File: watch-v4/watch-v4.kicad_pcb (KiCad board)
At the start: 4 copper layers, 35 x 35 mm, 33 parts, among them J1 CONN_10, P1 array connection, Q1 MOSFET_P, SW1 SPST, SW2 SPST, SW3 SPST, U1 IC_MCP73831, U2 MAX1722, U3 DS3231, U4 LSM9DS0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

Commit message: schematic cleanup, board work
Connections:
- net Net-(D2-Pad2) renamed /STAT
- D1 pad 1: Net-(D1-Pad1) -> /EXTVCC
- D1 pad 2: Net-(D1-Pad2) -> /Regulator_In
- J1 pad 4: Net-(J1-Pad4) -> VCC
- L1 pad 1: Net-(D1-Pad2) -> /Regulator_In
- P1 pad 1: EXTVCC -> /EXTVCC
- Q1 pad 1: EXTVCC -> /EXTVCC
- Q1 pad 3: Net-(D1-Pad2) -> /Regulator_In
- R1 pad 2: EXTVCC -> /EXTVCC
- R3 pad 1: Net-(D1-Pad1) -> /EXTVCC
- U1 pad 4: EXTVCC -> /EXTVCC
- U2 pad 1: Net-(D1-Pad2) -> /Regulator_In
- U2 pad 3: Net-(U2-Pad3) -> /Regulator_In
- XL1 pad 1: EXTVCC -> /EXTVCC
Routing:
- net /EXTVCC: track 0.00 -> 50.4 mm, vias 0 -> 1
- net EXTVCC: track 47.2 -> 0.00 mm, vias 1 -> 0
- net /Regulator_In: track 0.00 -> 15.7 mm
- net Net-(D1-Pad2): track 11.6 -> 0.00 mm
- net Net-(D1-Pad1): track 3.24 -> 0.00 mm
- net VCC: track 113.7 -> 114.2 mm

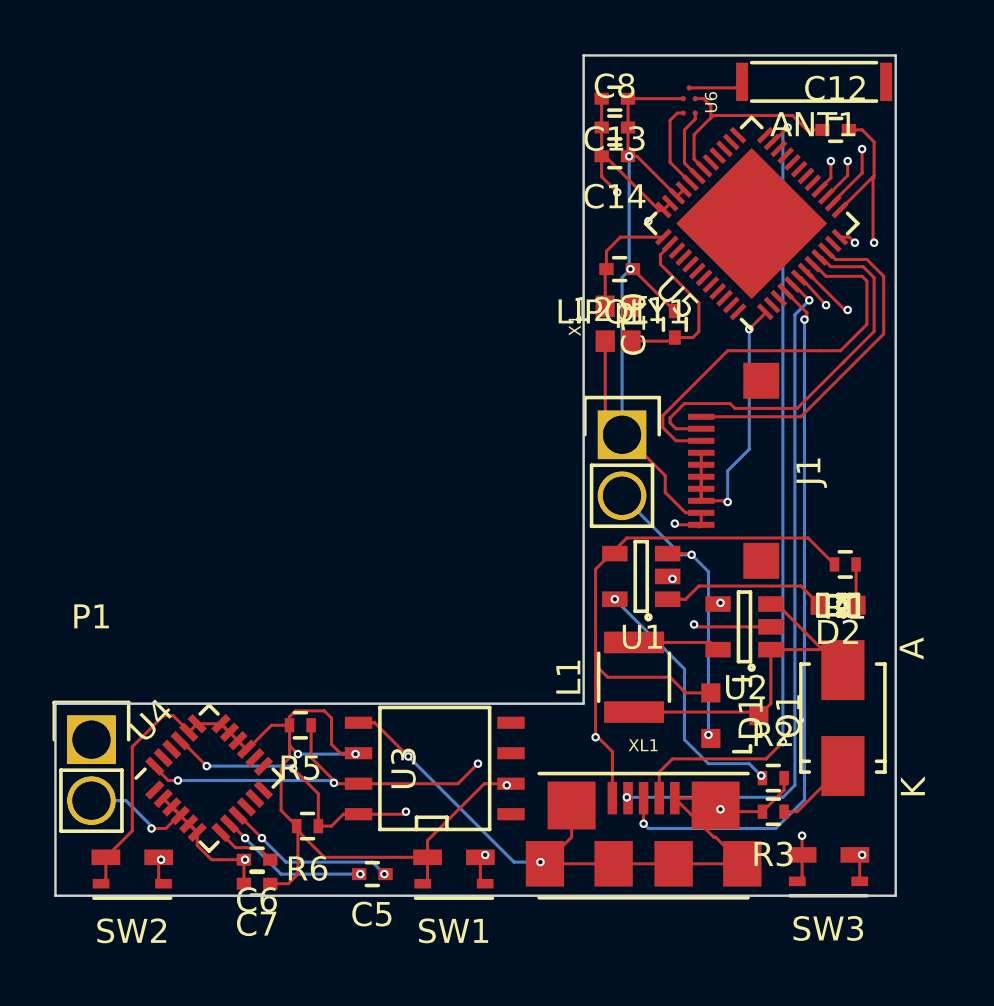
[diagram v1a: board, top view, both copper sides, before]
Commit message: re-route board, redraw power supply in schematic
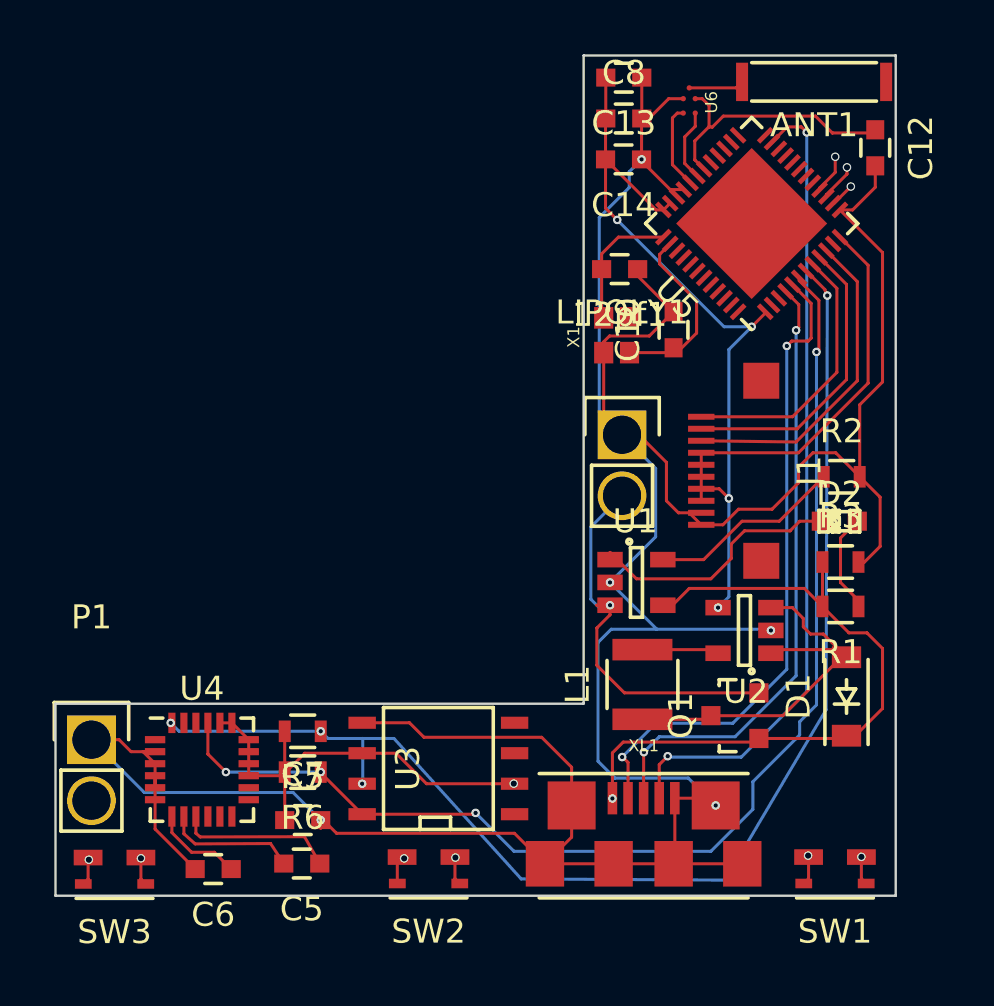
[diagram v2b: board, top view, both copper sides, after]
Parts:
- 12pf1, C10, C12, C13, C14, C5, C6, C7, C8: footprint Capacitors_SMD:C_0402 -> Capacitors_SMD:C_0603
- D1: footprint Diodes_SMD:Diode-SMA_Standard -> Diodes_SMD:SOD-123
- R1, R2, R3, R5, R6: footprint Resistors_SMD:R_0402 -> Resistors_SMD:R_0603
- moved SW3 29.7 mm to (152.7, 114.4)
- moved SW1 15.9 mm to (182.7, 114.4)
- moved R2 12.9 mm to (182.9, 98.2)
- moved SW2 12.3 mm to (165.7, 114.4)
- moved R3 10.8 mm to (182.9, 101.8), turned to 0 degrees
- moved D2 3.50 mm to (182.8, 100.1), turned to 0 degrees
- moved C7 3.26 mm to (160.5, 112.5), turned to 0 degrees
- moved C5 2.97 mm to (160.5, 114.4)
- moved R6 2.26 mm to (160.5, 110.5)
- moved C6 1.87 mm to (156.8, 114.6)
- moved C12 1.81 mm to (184.3, 84.5), turned to 270 degrees
- moved R1 1.76 mm to (182.9, 103.7)
- moved C13 0.95 mm to (173.9, 81.6)
- moved D1 0.91 mm to (183.2, 107.4)
- moved C8 0.53 mm to (173.9, 83.3)
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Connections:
- net Net-(LIPOLY1-Pad2) renamed /VBAT
- D2 pad 2: /STAT -> Net-(D2-Pad2)
- P1 pad 1: /EXTVCC -> GND
- P1 pad 2: GND -> /EXTVCC
- R1 pad 1: Net-(D2-Pad1) -> Net-(D2-Pad2)
- U1 pad 1: /STAT -> Net-(D2-Pad1)
- U5 pad 10: DISPLAY_SCK -> DISPLAY_SS
- U5 pad 8: DISPLAY_SS -> DISPLAY_SCK
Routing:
- net GND: track 128.8 -> 150.3 mm, vias 11 -> 5
- net Net-(SW3-Pad2): track 35.3 -> 52.4 mm
- net Net-(SW1-Pad2): track 44.5 -> 30.3 mm
- net Net-(SW2-Pad2): track 53.4 -> 39.3 mm
- net VCC: track 114.2 -> 127.8 mm, vias 10 -> 8
- net Net-(D2-Pad1): track 1.70 -> 10.9 mm
- net /STAT: track 6.91 -> 0.00 mm
- net SDA: track 50.2 -> 54.8 mm
- net Net-(D2-Pad2): track 0.00 -> 4.33 mm
- net DISPLAY_MOSI: track 16.8 -> 12.4 mm
- net /TX: track 29.9 -> 25.9 mm
- net /VBAT: track 13.4 -> 17.4 mm, vias 2 -> 1
- net DISPLAY_SS: track 16.7 -> 13.5 mm
- net DISPLAY_SCK: track 14.3 -> 11.3 mm
- net Net-(R2-Pad1): track 11.0 -> 8.13 mm, vias 2 -> 0
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
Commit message: forgot to netlist the new parts; now with more caps, connections
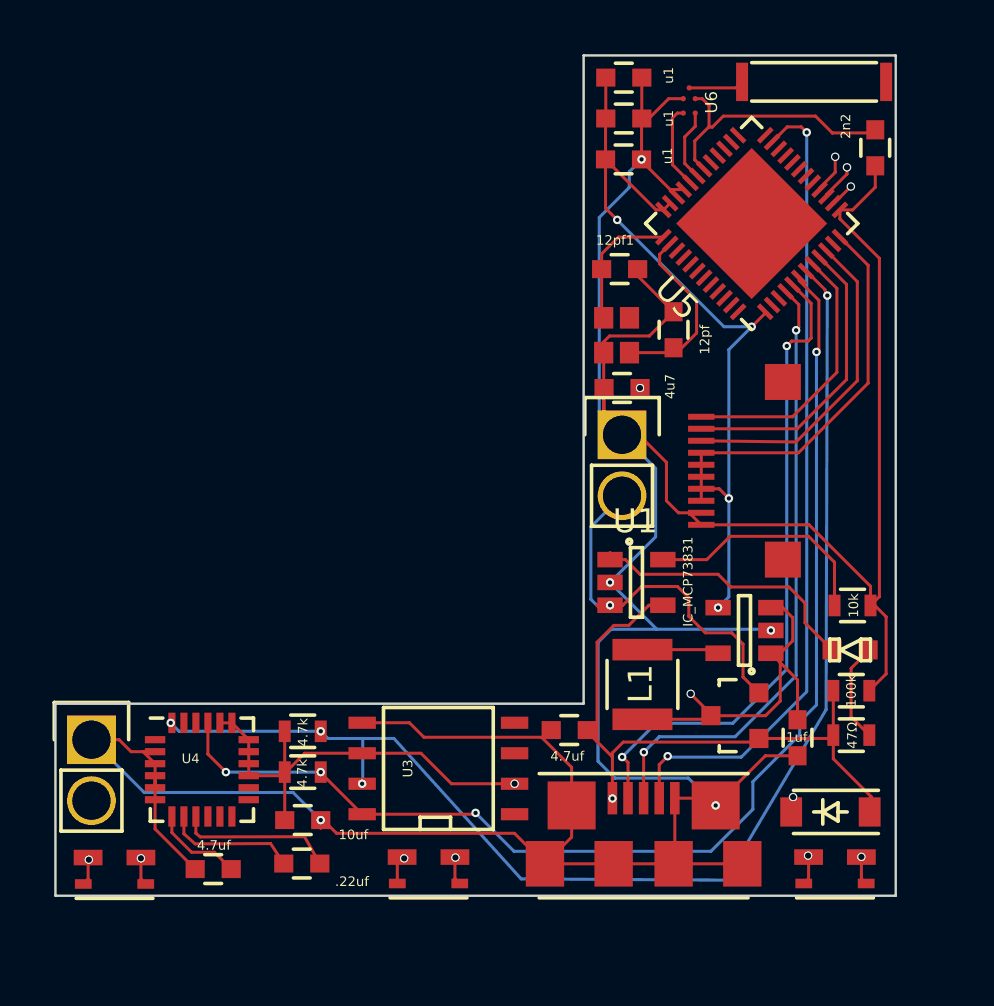
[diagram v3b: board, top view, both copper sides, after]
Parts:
- added C1: 1uf, Capacitors_SMD:C_0603, F.Cu at (181.1, 109.1)
- added C2: 4.7uf, Capacitors_SMD:C_0603, F.Cu at (171.6, 108.8)
- added C3: 4u7, Capacitors_SMD:C_0603, F.Cu at (173.8, 94.5)
- C12: value 2.2nf -> 2n2
- C13, C14, C8: value 0.1uf -> u1
- D2: footprint LEDs:LED-0603 -> LED-0603
- J1: footprint watch-v4:omron_XF2M-1015-1A -> watch-v4:omron_XF2M-1015-1A-2
- R2: value 10kΩ -> 10k
- R3: value R100kΩ -> 100k
- moved D2 5.38 mm to (183.3, 105.5)
- moved R2 5.38 mm to (183.4, 103.6)
- moved R1 5.38 mm to (183.3, 109.0)
- moved R3 5.38 mm to (183.3, 107.2)
- moved D1 4.86 mm to (182.5, 112.2), turned to 180 degrees
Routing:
- net GND: track 150.3 -> 161.9 mm
- net /Regulator_In: track 17.1 -> 22.5 mm, vias 0 -> 2
- net /VBAT: track 17.4 -> 22.7 mm, vias 1 -> 2
- net /EXTVCC: track 50.5 -> 48.4 mm
- net Net-(R2-Pad1): track 8.13 -> 9.80 mm
- net VCC: track 127.8 -> 126.4 mm
- net Net-(D2-Pad1): track 10.9 -> 11.6 mm

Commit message: really should have commited this months ago...
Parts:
- C12: value 2n2 -> 2.2nf
- C13, C14, C8: value u1 -> 0.1uf
- C3: value 4u7 -> 4.7uf
- R2: value 10k -> 10kΩ
- R3: value 100k -> R100kΩ
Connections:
- J1 pad 4: VCC -> Net-(J1-Pad4)
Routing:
- net GND: track 161.9 -> 144.6 mm
- net DISPLAY_SS: track 13.5 -> 16.6 mm, vias 0 -> 2
- net VCC: track 126.4 -> 129.0 mm, vias 8 -> 9
- net DISPLAY_MOSI: track 12.4 -> 13.4 mm
- net DISPLAY_SCK: track 11.3 -> 11.9 mm, vias 0 -> 2
- added copper zone on B.Cu, net GND
- added copper zone on F.Cu, net GND
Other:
- net class power added: clearance 0.127, trace_width 0.2, via_dia 0.355, via_drill 0.254
- board text added: "Ourglass Rev 4.2"
